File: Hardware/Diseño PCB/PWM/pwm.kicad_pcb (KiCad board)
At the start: 2 copper layers, 100 x 80 mm, 38 parts, among them J1 VE, J2 Vo, Q3 IRF540N, Q4 IRF540N, U2 IR2111

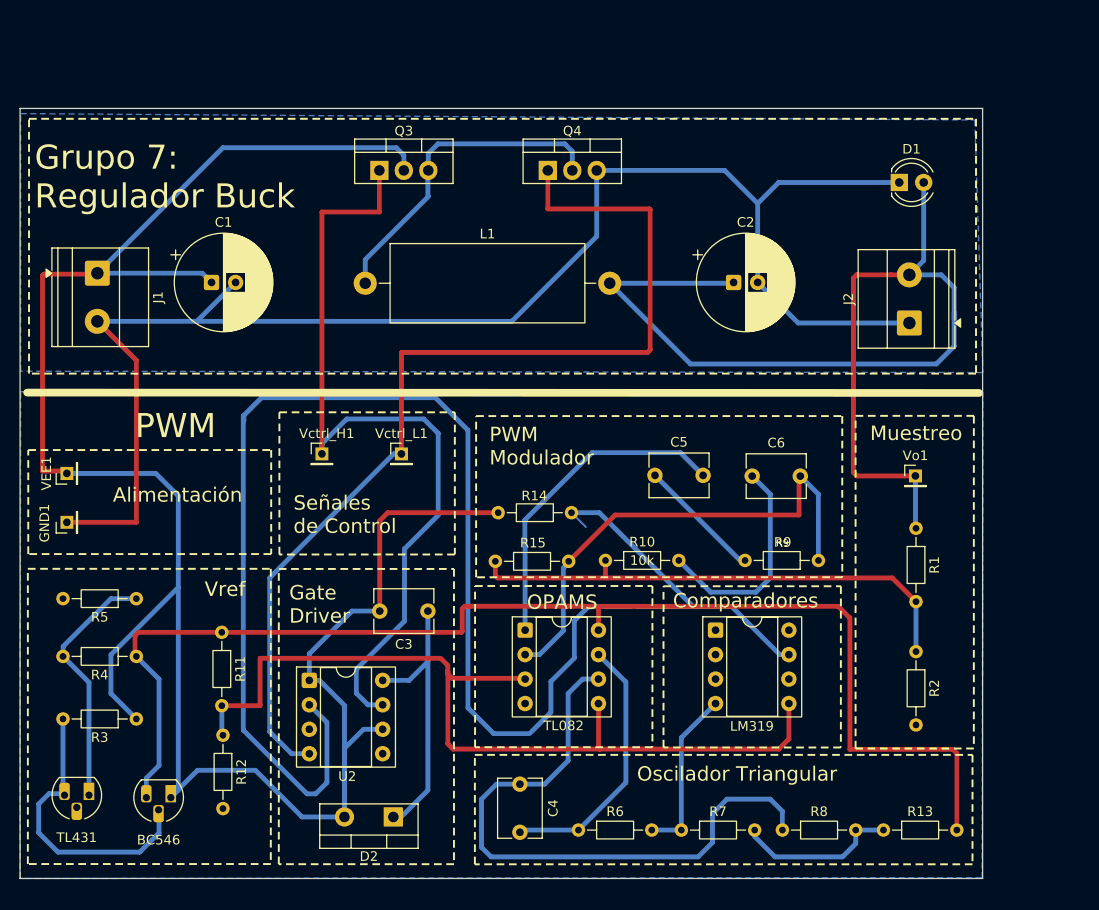
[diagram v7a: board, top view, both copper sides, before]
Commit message: CHK4: Correccion pcb NMOS
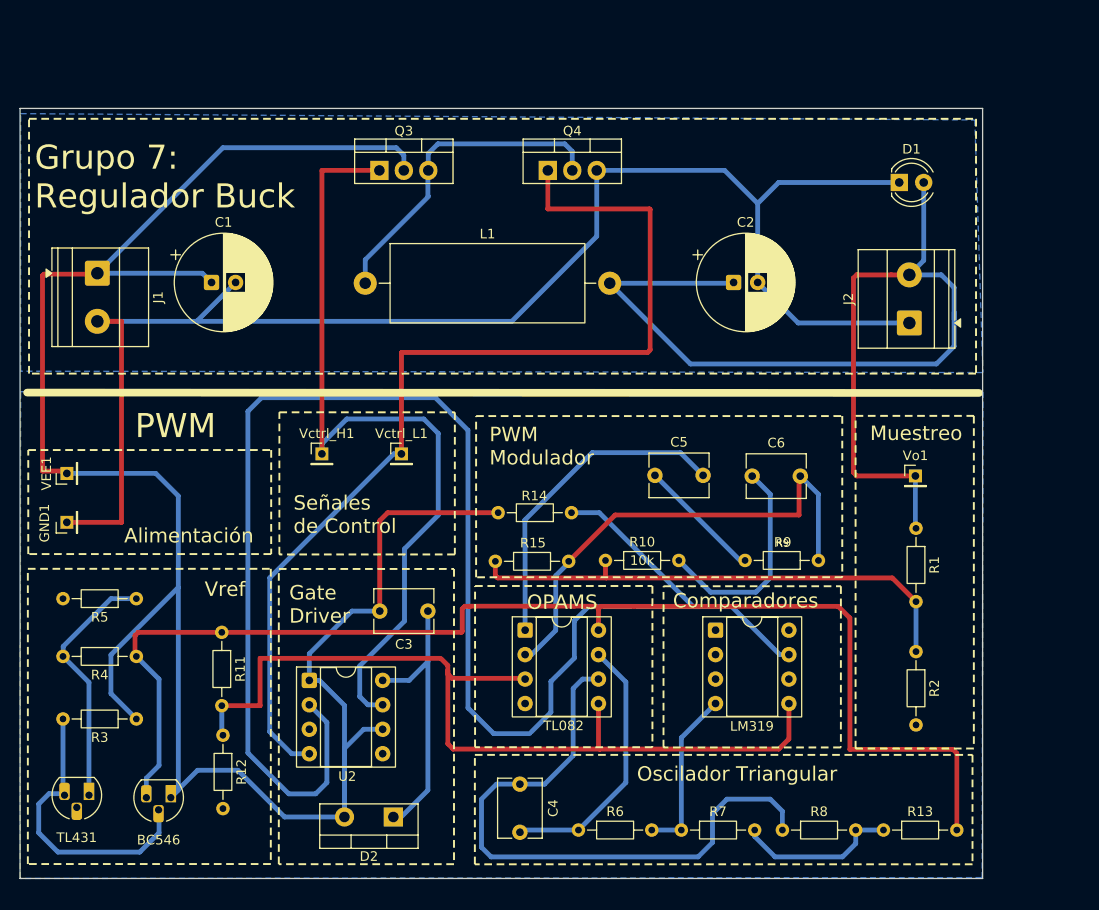
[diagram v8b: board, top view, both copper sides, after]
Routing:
- net /PWM: track 174.0 -> 172.0 mm
- net GND: track 157.6 -> 156.9 mm
